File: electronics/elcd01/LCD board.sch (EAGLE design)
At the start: 5 parts, among them SW1 ENCODER_SW1-PEC12, X1 HD44780LCD-1602

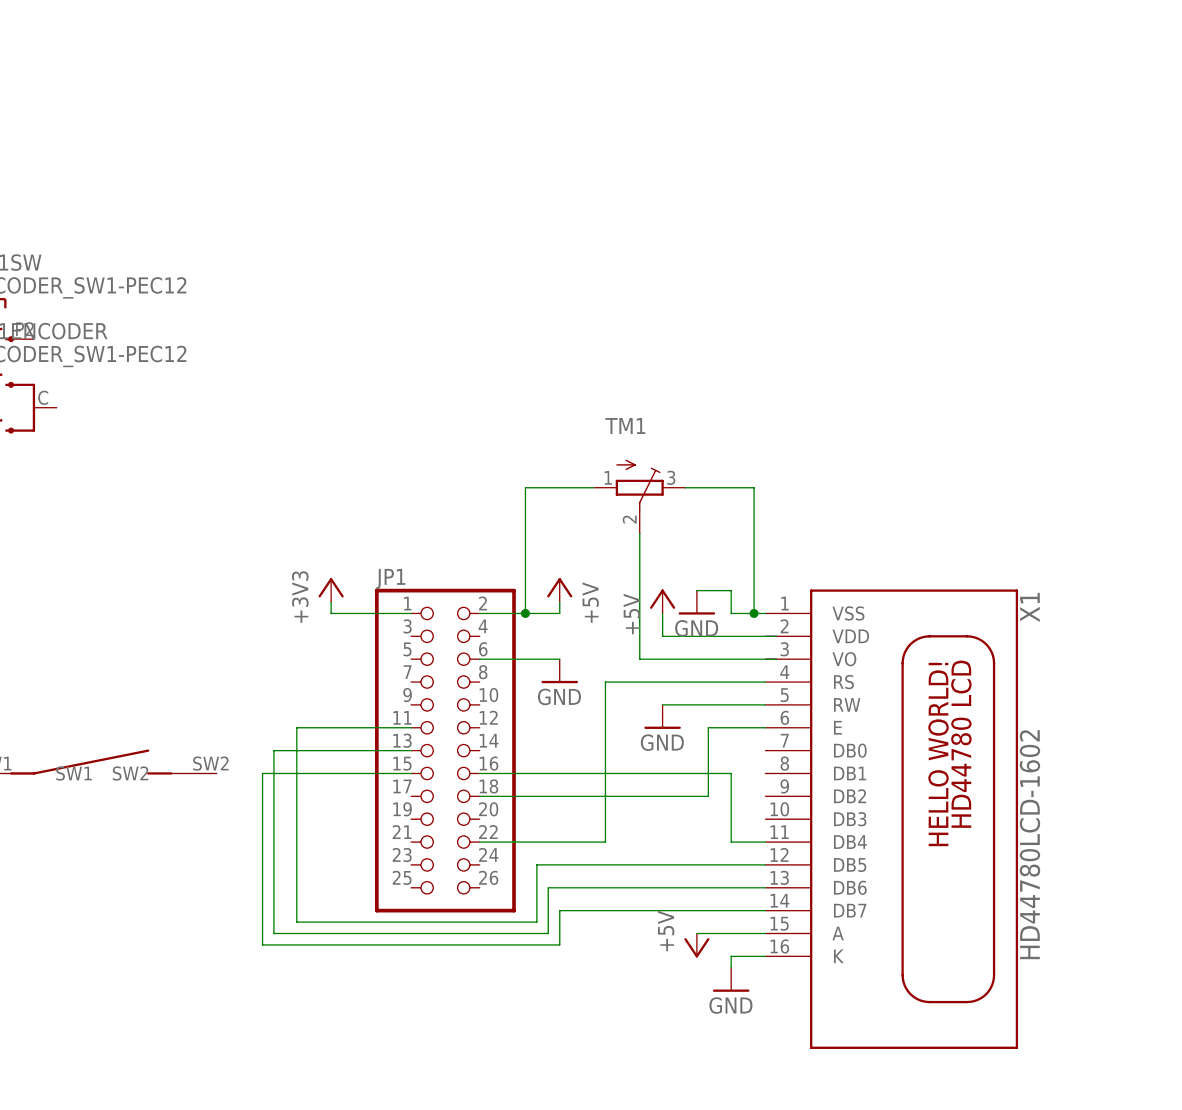
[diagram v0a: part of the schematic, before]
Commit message: Changed connector on LCD board.  Added notes to EMC01 board.
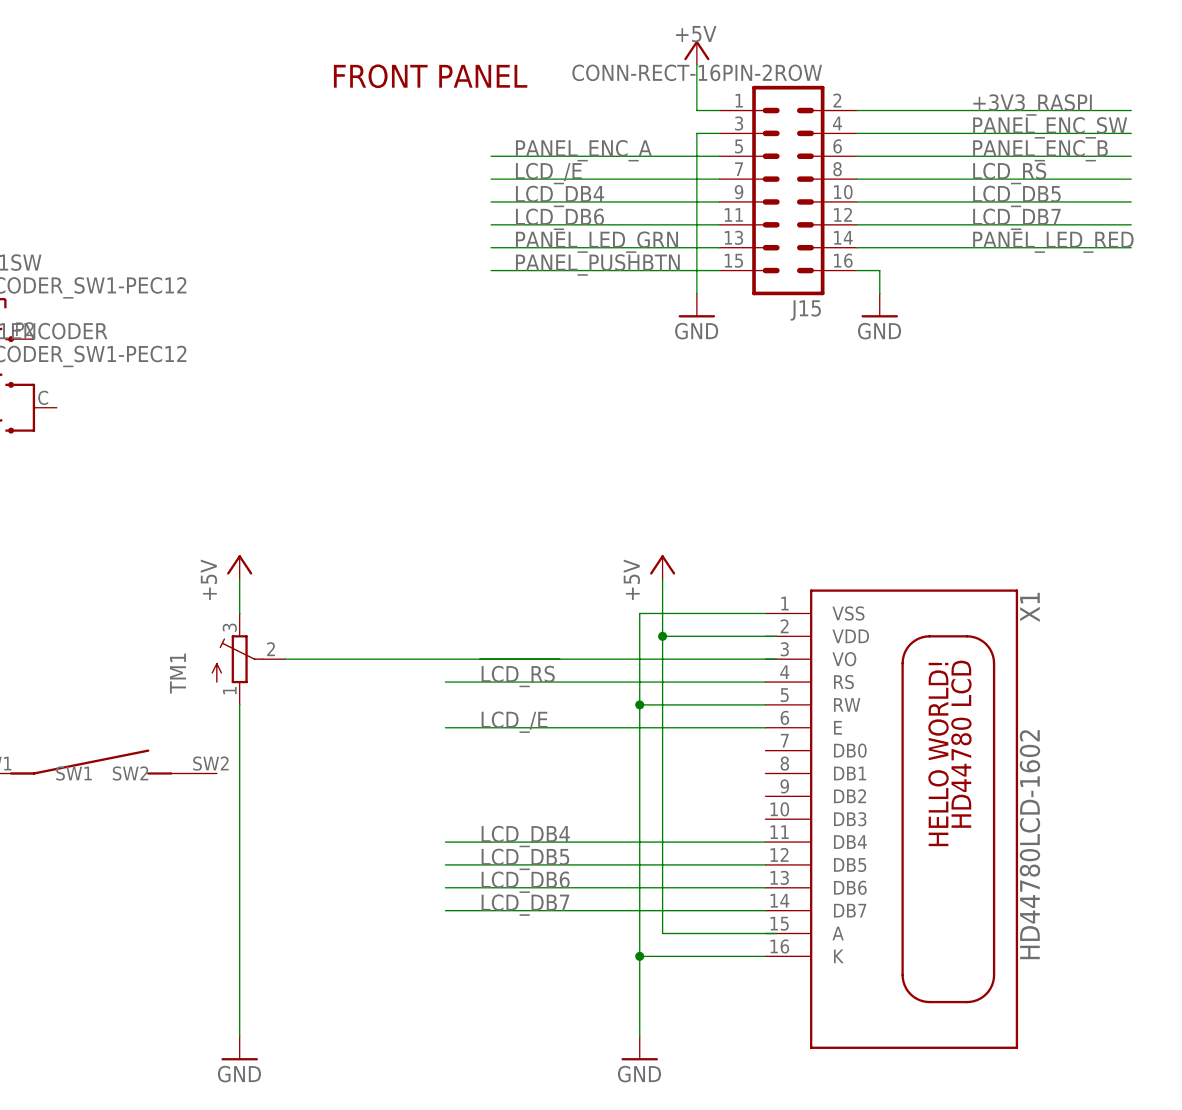
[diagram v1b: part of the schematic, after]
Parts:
- removed JP1: (no value), pinhead-2:PINHD-2X13_2.54-SMD
- added J15: CONN-RECT-16PIN-2ROW, FirePick:CONN-RECT-16PIN-2ROW
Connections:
- removed net +3V3: JP1.1
- removed net N$2: JP1.16, X1.DB4
- removed net N$3: JP1.22, X1.RS
- removed net N$4: JP1.11, X1.DB5
- removed net N$5: JP1.13, X1.DB6
- removed net N$6: JP1.18, X1.E
- removed net N$7: JP1.15, X1.DB7
- new net +3V3_RASPI: J15.2
- new net LCD_/E: J15.7, X1.E
- new net LCD_DB4: J15.9, X1.DB4
- new net LCD_DB5: J15.10, X1.DB5
- new net LCD_DB6: J15.11, X1.DB6
- new net LCD_DB7: J15.12, X1.DB7
- new net LCD_RS: J15.8, X1.RS
- new net PANEL_ENC_A: J15.5
- new net PANEL_ENC_B: J15.6
- new net PANEL_ENC_SW: J15.4
- new net PANEL_LED_GRN: J15.13
- new net PANEL_LED_RED: J15.14
- new net PANEL_PUSHBTN: J15.15
- net +5V: now also J15.1, TM1.E; no longer JP1.2, TM1.A
- net GND: now also J15.16, J15.3, TM1.A; no longer JP1.6, TM1.E
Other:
- note added: "FRONT PANEL"
- moved on the sheet: TM1

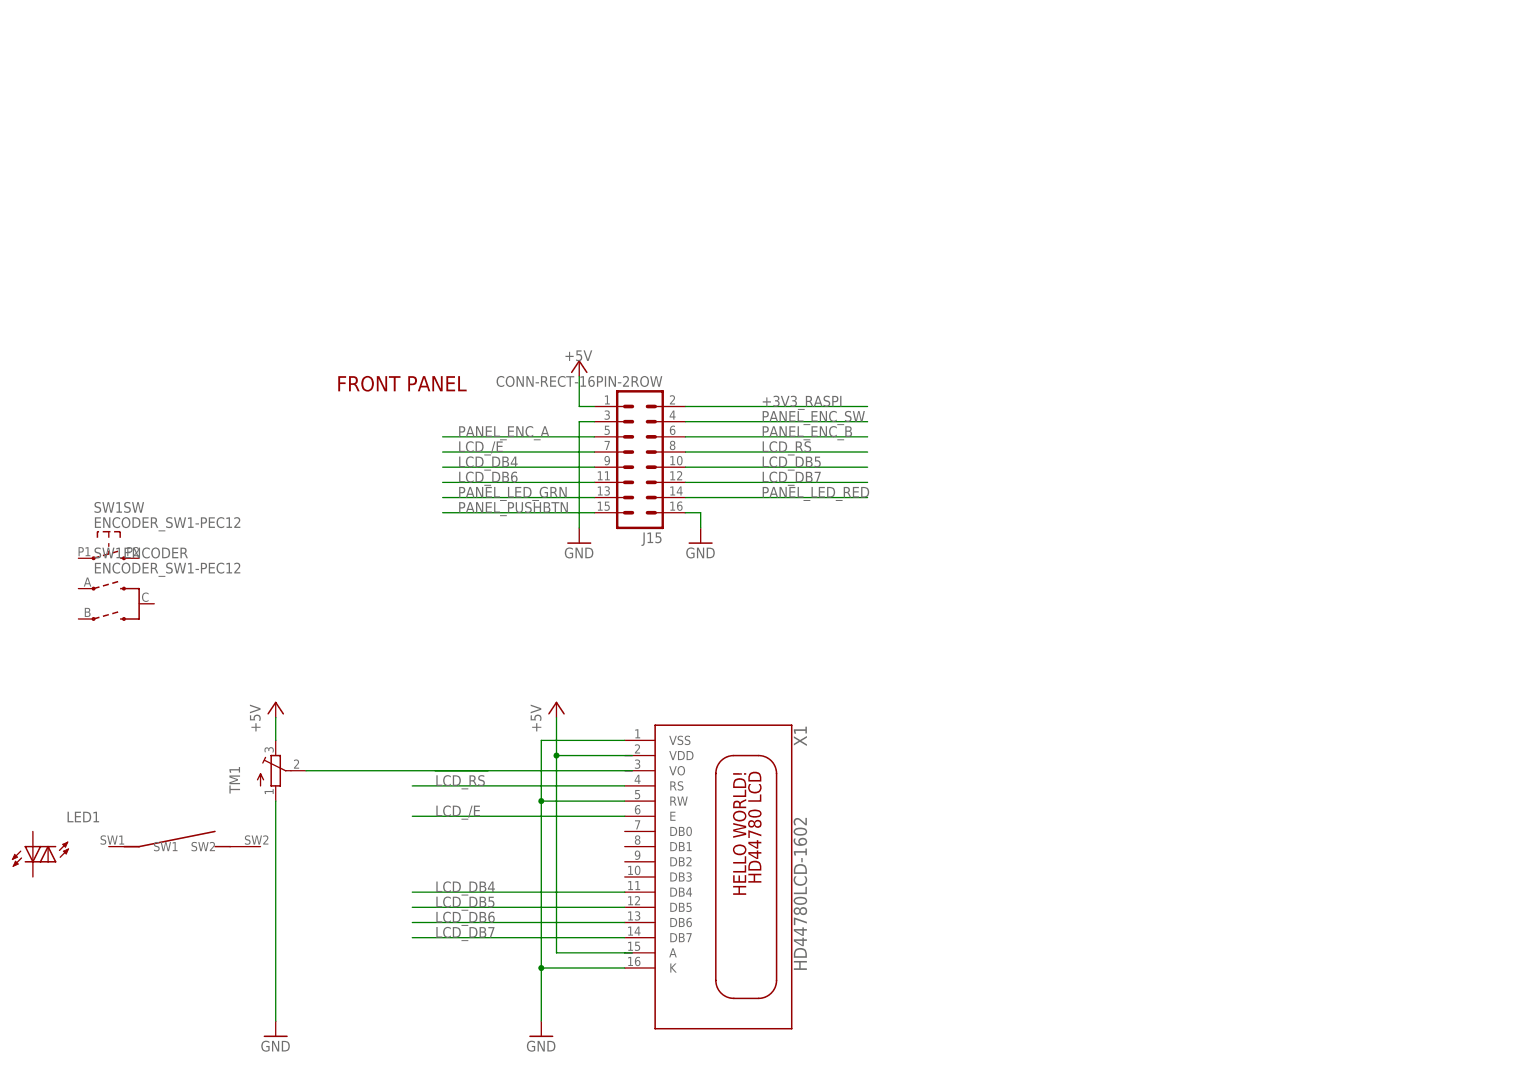
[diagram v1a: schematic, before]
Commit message: Wired up encoder, switches, and LEDs
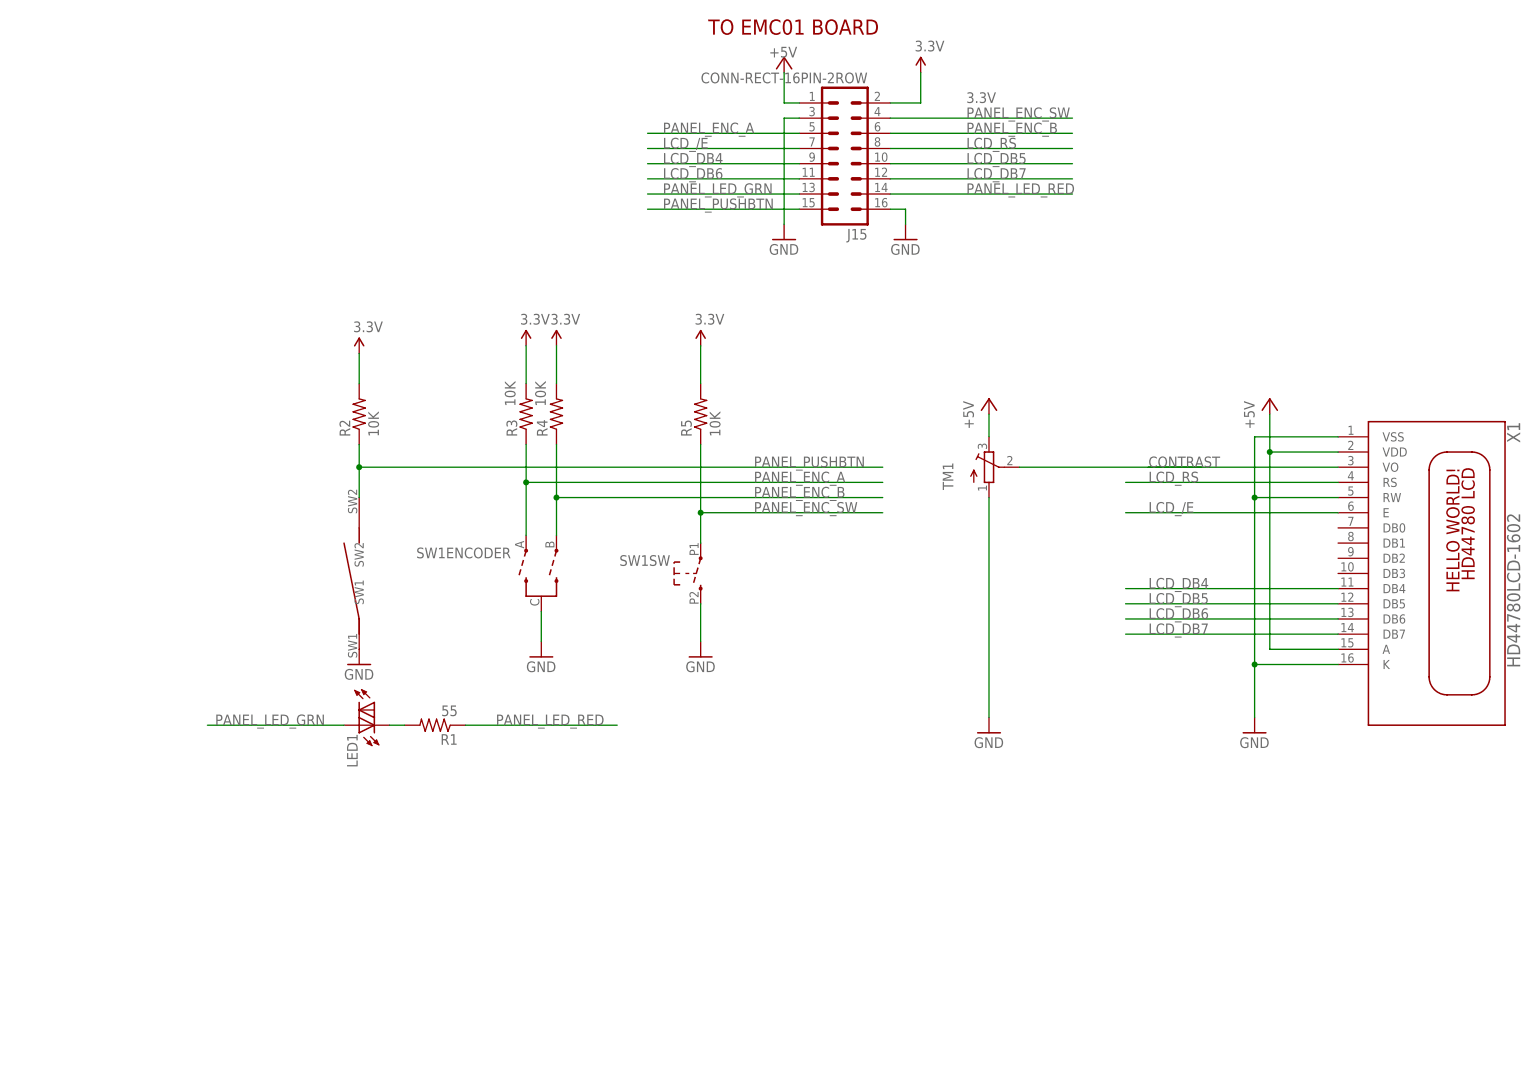
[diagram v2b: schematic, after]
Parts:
- added R1: 55, SparkFun-Passives:RESISTOR0805-RES
- added R2, R3, R4, R5: 10K, SparkFun-Passives:RESISTOR0805-RES
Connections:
- removed net +3V3_RASPI: J15.2
- new net 3.3V: J15.2, R2.2, R3.2, R4.2, R5.2
- new net N$2: LED1.C, R1.2
- net +5V: now also X1.VDD
- net GND: now also LED1.SW1, SW1ENCODER.C, SW1SW.2
- net N$1: now also X1.VO
- net PANEL_ENC_A: now also R3.1, SW1ENCODER.A
- net PANEL_ENC_B: now also R4.1, SW1ENCODER.B
- net PANEL_ENC_SW: now also R5.1, SW1SW.1
- net PANEL_LED_GRN: now also LED1.A
- net PANEL_LED_RED: now also R1.1
- net PANEL_PUSHBTN: now also LED1.SW2, R2.1
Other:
- note added: "TO EMC01 BOARD"
- note removed: "FRONT PANEL"
- moved on the sheet: J15, LED1, SW1ENCODER, SW1SW, TM1, X1
